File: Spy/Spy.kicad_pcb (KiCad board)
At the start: 2 copper layers, 8 parts, among them J1 Screw_Terminal_01x02, J2 Screw_Terminal_01x02, U1 ESP32-DevKitC, U2 GP2Y0A21YK0F, U3 GP2Y0A21YK0F, U4 SEN-12787, U5 L298N, U6 QTR-8A

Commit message: pcb edited
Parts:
- moved U5 48.9 mm to (94.2, 100.8), turned to 90 degrees
- moved J1 46.2 mm to (109.8, 86.0), turned to 180 degrees
- moved U1 39.6 mm to (130.1, 80.6)
- moved U2 39.1 mm to (107.7, 125.8)
- moved J2 31.8 mm to (85.0, 95.8), turned to -90 degrees
- moved U4 25.3 mm to (80.8, 116.5), turned to 90 degrees
- moved U3 24.3 mm to (97.7, 125.8)
- moved U6 15.0 mm to (135.0, 136.8)
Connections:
- J1 pad 1: unconnected-(J1-Pin_1-Pad1) -> Net-(J1-Pin_1)
- J1 pad 2: unconnected-(J1-Pin_2-Pad2) -> Net-(J1-Pin_2)
- J2 pad 1: unconnected-(J2-Pin_1-Pad1) -> Net-(J2-Pin_1)
- J2 pad 2: unconnected-(J2-Pin_2-Pad2) -> Net-(J2-Pin_2)
- U1 pad 1: unconnected-(U1-3V3-Pad1) -> Net-(U1-3V3)
- U1 pad 10: unconnected-(U1-DAC_2/ADC2_CH9/GPIO26-Pad10) -> Net-(U1-DAC_2/ADC2_CH9/GPIO26)
- U1 pad 12: unconnected-(U1-MTMS/GPIO14/ADC2_CH6-Pad12) -> Net-(U1-MTMS/GPIO14/ADC2_CH6)
- U1 pad 13: unconnected-(U1-MTDI/GPIO12/ADC2_CH5-Pad13) -> Net-(U1-MTDI/GPIO12/ADC2_CH5)
- U1 pad 14: Net-(U1-GND-Pad14) -> GND
- U1 pad 15: unconnected-(U1-MTCK/GPIO13/ADC2_CH4-Pad15) -> Net-(U1-MTCK/GPIO13/ADC2_CH4)
- U1 pad 19: unconnected-(U1-5V-Pad19) -> Net-(U1-5V)
- U1 pad 20: unconnected-(U1-SD_CLK/GPIO6-Pad20) -> Net-(U1-SD_CLK/GPIO6)
- U1 pad 21: unconnected-(U1-SD_DATA0/GPIO7-Pad21) -> Net-(U1-SD_DATA0/GPIO7)
- U1 pad 27: unconnected-(U1-GPIO16-Pad27) -> Net-(U1-GPIO16)
- U1 pad 28: unconnected-(U1-GPIO17-Pad28) -> Net-(U1-GPIO17)
- U1 pad 3: unconnected-(U1-SENSOR_VP/GPIO36/ADC1_CH0-Pad3) -> Net-(U1-SENSOR_VP/GPIO36/ADC1_CH0)
- U1 pad 30: unconnected-(U1-GPIO18-Pad30) -> Net-(U1-GPIO18)
- U1 pad 31: unconnected-(U1-GPIO19-Pad31) -> Net-(U1-GPIO19)
- U1 pad 32: Net-(U1-GND-Pad14) -> GND
- U1 pad 33: unconnected-(U1-GPIO21-Pad33) -> Net-(U1-GPIO21)
- U1 pad 36: unconnected-(U1-GPIO22-Pad36) -> Net-(U1-GPIO22)
- U1 pad 38: Net-(U1-GND-Pad14) -> GND
- U1 pad 5: unconnected-(U1-VDET_1/GPIO34/ADC1_CH6-Pad5) -> Net-(U1-VDET_1/GPIO34/ADC1_CH6)
- U1 pad 6: unconnected-(U1-VDET_2/GPIO35/ADC1_CH7-Pad6) -> Net-(U1-VDET_2/GPIO35/ADC1_CH7)
- U1 pad 7: unconnected-(U1-32K_XP/GPIO32/ADC1_CH4-Pad7) -> Net-(U1-32K_XP/GPIO32/ADC1_CH4)
- U1 pad 8: unconnected-(U1-32K_XN/GPIO33/ADC1_CH5-Pad8) -> Net-(U1-32K_XN/GPIO33/ADC1_CH5)
- U1 pad 9: unconnected-(U1-DAC_1/ADC2_CH8/GPIO25-Pad9) -> Net-(U1-DAC_1/ADC2_CH8/GPIO25)
- U2 pad 1: unconnected-(U2-GND-Pad1) -> GND
- U2 pad 2: unconnected-(U2-VCC-Pad2) -> Net-(U1-3V3)
- U2 pad 3: unconnected-(U2-VOUT-Pad3) -> Net-(U1-DAC_1/ADC2_CH8/GPIO25)
- U3 pad 1: unconnected-(U3-GND-Pad1) -> GND
- U3 pad 2: unconnected-(U3-VCC-Pad2) -> Net-(U1-3V3)
- U3 pad 3: unconnected-(U3-VOUT-Pad3) -> Net-(U1-DAC_2/ADC2_CH9/GPIO26)
- U4 pad 2: unconnected-(U4-GND-Pad2) -> GND
- U4 pad 3: unconnected-(U4-VCC-Pad3) -> Net-(U1-3V3)
- U4 pad 4: unconnected-(U4-SDA-Pad4) -> Net-(U1-SD_DATA0/GPIO7)
- U4 pad 5: unconnected-(U4-SCL-Pad5) -> Net-(U1-SD_CLK/GPIO6)
- U5 pad 10: unconnected-(U5-IN3-Pad10) -> Net-(U1-GPIO18)
- U5 pad 11: unconnected-(U5-ENB-Pad11) -> Net-(U1-GPIO22)
- U5 pad 12: unconnected-(U5-IN4-Pad12) -> Net-(U1-GPIO19)
- U5 pad 13: unconnected-(U5-OUT3-Pad13) -> Net-(J1-Pin_1)
- U5 pad 14: unconnected-(U5-OUT4-Pad14) -> Net-(J1-Pin_2)
- U5 pad 2: unconnected-(U5-OUT1-Pad2) -> Net-(J2-Pin_1)
- U5 pad 3: unconnected-(U5-OUT2-Pad3) -> Net-(J2-Pin_2)
- U5 pad 4: unconnected-(U5-VS-Pad4) -> Net-(U1-5V)
- U5 pad 5: unconnected-(U5-IN1-Pad5) -> Net-(U1-GPIO16)
- U5 pad 6: unconnected-(U5-ENA-Pad6) -> Net-(U1-GPIO21)
- U5 pad 7: unconnected-(U5-IN2-Pad7) -> Net-(U1-GPIO17)
- U5 pad 8: unconnected-(U5-GND-Pad8) -> GND
- U5 pad 9: unconnected-(U5-VSS-Pad9) -> +12V
- U6 pad 3V3: unconnected-(U6-Pad3V3) -> Net-(U1-3V3)
- U6 pad GND: unconnected-(U6-PadGND) -> GND
- U6 pad LED1: unconnected-(U6-PadLED1) -> Net-(U1-SENSOR_VP/GPIO36/ADC1_CH0)
- U6 pad LED2: unconnected-(U6-PadLED2) -> Net-(U1-VDET_2/GPIO35/ADC1_CH7)
- U6 pad LED3: unconnected-(U6-PadLED3) -> Net-(U1-VDET_1/GPIO34/ADC1_CH6)
- U6 pad LED4: unconnected-(U6-PadLED4) -> Net-(U1-MTMS/GPIO14/ADC2_CH6)
- U6 pad LED5: unconnected-(U6-PadLED5) -> Net-(U1-MTCK/GPIO13/ADC2_CH4)
- U6 pad LED6: unconnected-(U6-PadLED6) -> Net-(U1-MTDI/GPIO12/ADC2_CH5)
- U6 pad LED7: unconnected-(U6-PadLED7) -> Net-(U1-32K_XN/GPIO33/ADC1_CH5)
- U6 pad LED8: unconnected-(U6-PadLED8) -> Net-(U1-32K_XP/GPIO32/ADC1_CH4)
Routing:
- net GND: track 0.00 -> 197.8 mm
- net Net-(U1-5V): track 0.00 -> 107.5 mm
- net Net-(U1-SD_CLK/GPIO6): track 0.00 -> 100.1 mm
- net Net-(U1-3V3): track 0.00 -> 99.0 mm
- net Net-(U1-GPIO18): track 0.00 -> 97.8 mm, vias 0 -> 1
- net Net-(U1-SD_DATA0/GPIO7): track 0.00 -> 96.3 mm
- net Net-(U1-GPIO16): track 0.00 -> 75.3 mm, vias 0 -> 1
- net Net-(U1-GPIO21): track 0.00 -> 74.7 mm
- net Net-(U1-GPIO17): track 0.00 -> 70.3 mm, vias 0 -> 1
- net Net-(U1-VDET_1/GPIO34/ADC1_CH6): track 0.00 -> 70.3 mm
- net Net-(U1-GPIO19): track 0.00 -> 64.3 mm, vias 0 -> 1
- net Net-(U1-SENSOR_VP/GPIO36/ADC1_CH0): track 0.00 -> 61.3 mm
- net Net-(U1-GPIO22): track 0.00 -> 60.0 mm, vias 0 -> 1
- net Net-(U1-VDET_2/GPIO35/ADC1_CH7): track 0.00 -> 58.5 mm
- net Net-(U1-DAC_2/ADC2_CH9/GPIO26): track 0.00 -> 48.3 mm
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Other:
- board outline added: 96.8 x 80 mm

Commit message: new pcb
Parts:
- moved U4 96.0 mm to (174.8, 97.0), turned to -90 degrees
- moved J2 91.7 mm to (175.5, 80.8), turned to 180 degrees
- moved U6 75.8 mm to (63.0, 113.0), turned to -90 degrees
- moved J1 67.2 mm to (171.2, 113.2), turned to 0 degrees
- moved U2 66.4 mm to (73.2, 69.0)
- moved U1 63.7 mm to (73.1, 109.2), turned to 90 degrees
- moved U3 58.3 mm to (108.5, 68.5)
- moved U5 42.4 mm to (134.5, 87.8), turned to 0 degrees
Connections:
- net Net-(U1-32K_XN/GPIO33/ADC1_CH5) renamed GPIO33
- net Net-(U1-32K_XP/GPIO32/ADC1_CH4) renamed GPIO32
- net Net-(U1-3V3) renamed 3V3
- net Net-(U1-DAC_1/ADC2_CH8/GPIO25) renamed GPIO25
- net Net-(U1-DAC_2/ADC2_CH9/GPIO26) renamed GPIO26
- net Net-(U1-GPIO16) renamed GPIO16
- net Net-(U1-GPIO17) renamed GPIO17
- net Net-(U1-GPIO18) renamed GPIO18
- net Net-(U1-GPIO19) renamed GPIO19
- net Net-(U1-GPIO21) renamed GPIO21
- net Net-(U1-GPIO22) renamed GPIO22
- net Net-(U1-MTCK/GPIO13/ADC2_CH4) renamed GPIO13
- net Net-(U1-MTDI/GPIO12/ADC2_CH5) renamed GPIO12
- net Net-(U1-MTMS/GPIO14/ADC2_CH6) renamed GPIO14
- net Net-(U1-SD_CLK/GPIO6) renamed GPIO6
- net Net-(U1-SD_DATA0/GPIO7) renamed GPIO7
- net Net-(U1-SENSOR_VP/GPIO36/ADC1_CH0) renamed GPIO36
- net Net-(U1-VDET_1/GPIO34/ADC1_CH6) renamed GPIO34
- net Net-(U1-VDET_2/GPIO35/ADC1_CH7) renamed GPIO35
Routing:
- net 3V3: track 99.0 -> 216.1 mm
- net GND: track 197.8 -> 273.7 mm
- net Net-(U1-5V): track 107.5 -> 36.1 mm
- net GPIO18: track 97.8 -> 52.6 mm, vias 1 -> 0
- net GPIO16: track 75.3 -> 37.2 mm, vias 1 -> 0
- net Net-(J1-Pin_1): track 17.0 -> 47.5 mm
- net GPIO17: track 70.3 -> 40.8 mm, vias 1 -> 0
- net Net-(J2-Pin_1): track 10.4 -> 39.3 mm
- net Net-(J1-Pin_2): track 12.2 -> 40.5 mm
- net Net-(J2-Pin_2): track 13.9 -> 41.7 mm
- net GPIO13: track 26.1 -> 53.8 mm
- net GPIO26: track 48.3 -> 74.4 mm, vias 0 -> 1
- net GPIO34: track 70.3 -> 50.7 mm
- net GPIO12: track 32.0 -> 49.3 mm
- net GPIO32: track 47.4 -> 30.3 mm
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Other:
- board size 96.8 x 80 mm -> 134.2 x 76 mm

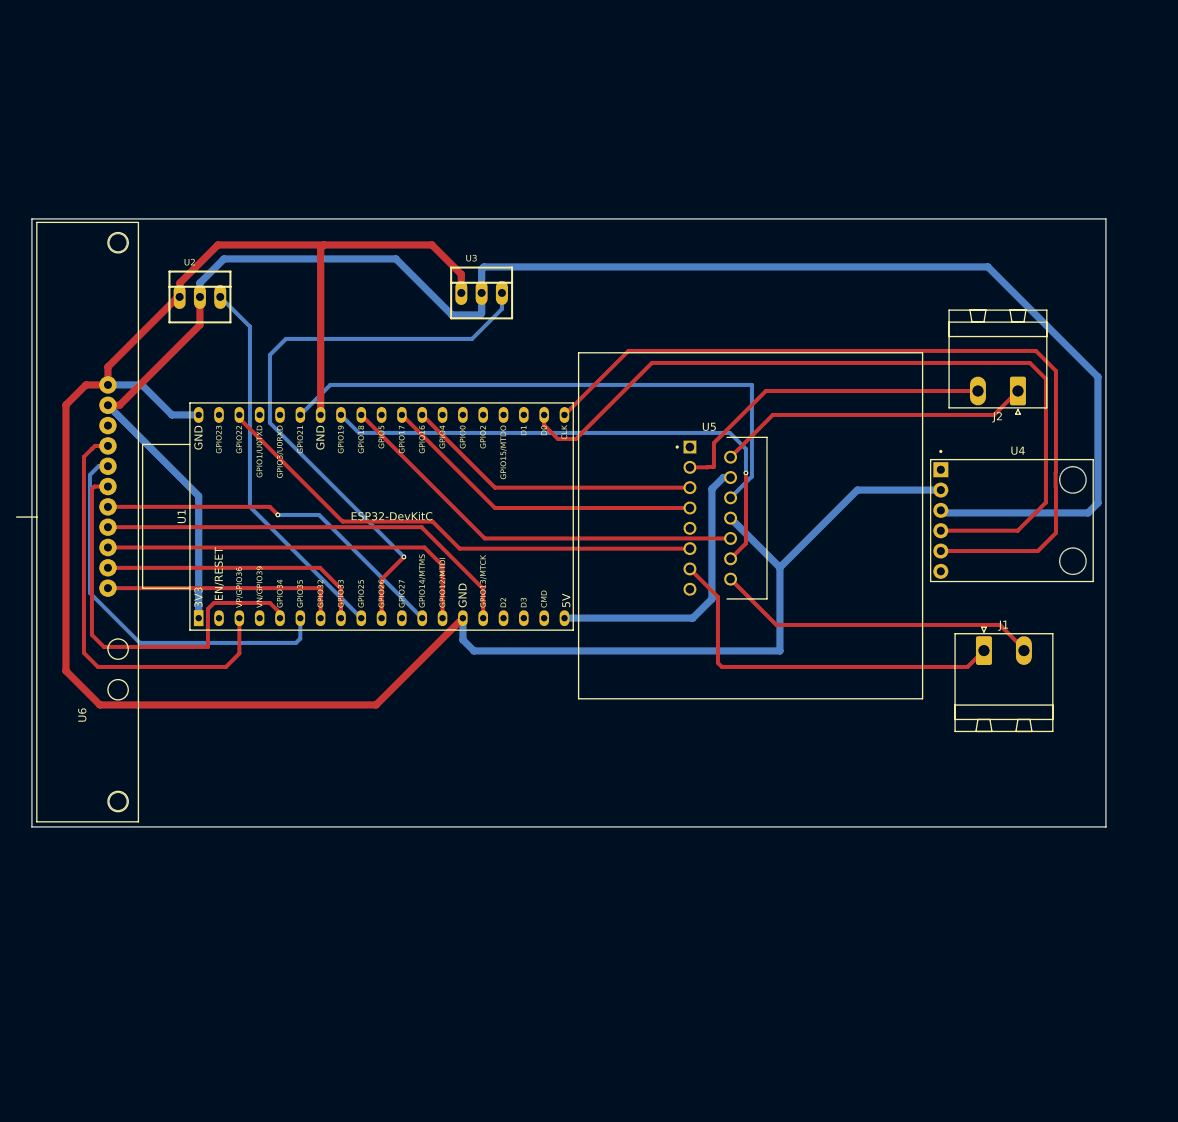
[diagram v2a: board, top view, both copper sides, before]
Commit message: DRV8871 driver and pin rewiring
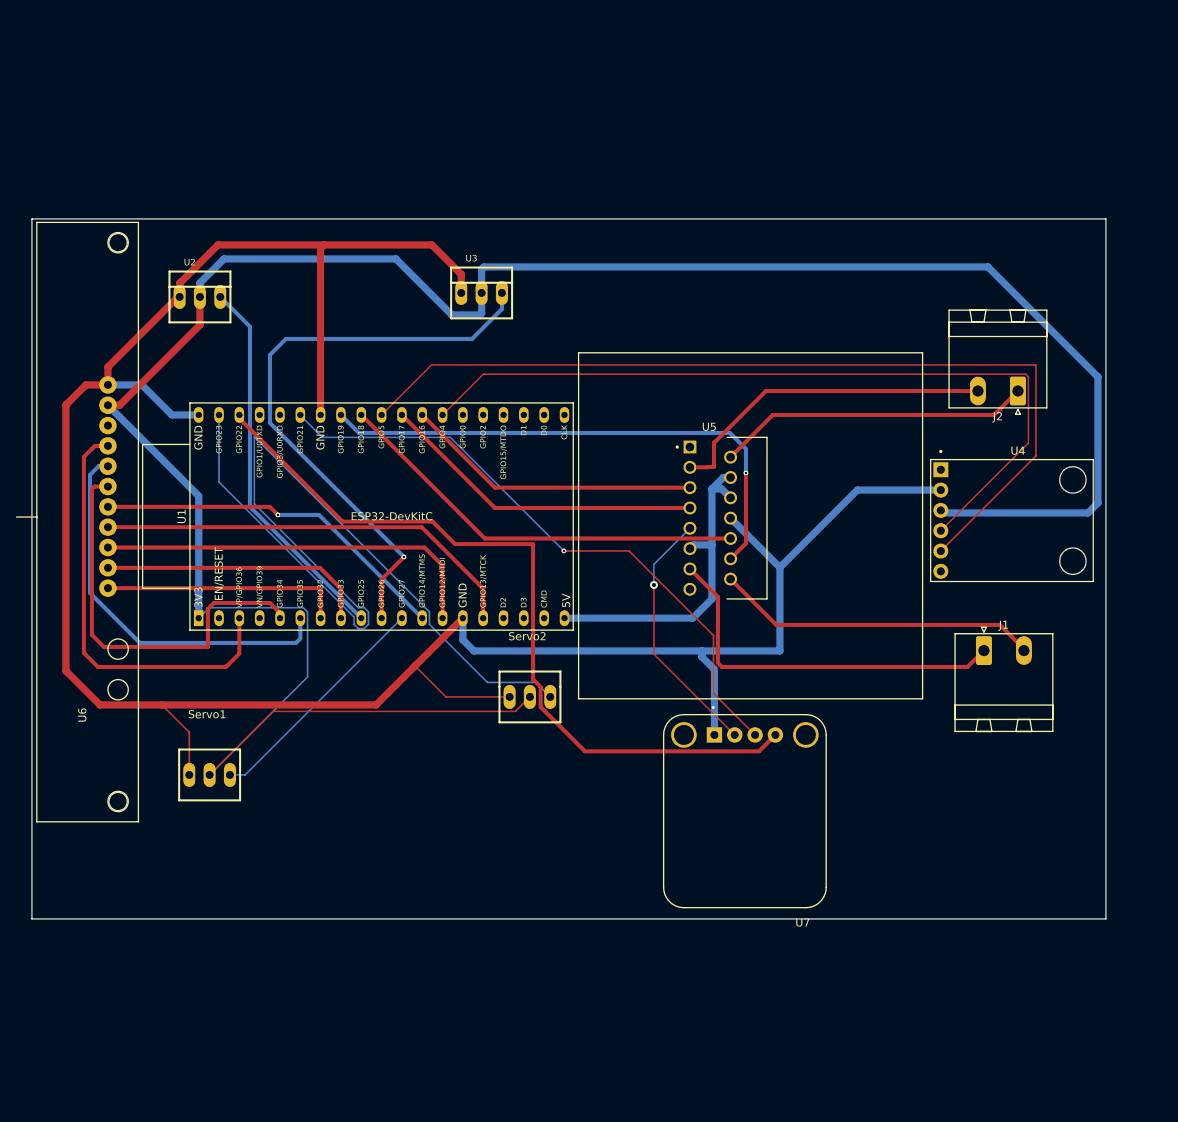
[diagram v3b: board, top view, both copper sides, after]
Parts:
- added Servo1: ~, FS5103B:FS5103B, F.Cu at (74.2, 121.7)
- added Servo2: ~, FS5103B:FS5103B, F.Cu at (114.2, 112.0)
- added U7: 3190, 3190:MODULE_3190, F.Cu at (141.4, 133.3)
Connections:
- U1 pad 11: unconnected-(U1-ADC2_CH7/GPIO27-Pad11) -> GPIO27
- U1 pad 20: GPIO6 -> unconnected-(U1-SD_CLK/GPIO6-Pad20)
- U1 pad 21: GPIO7 -> unconnected-(U1-SD_DATA0/GPIO7-Pad21)
- U1 pad 26: unconnected-(U1-ADC2_CH0/GPIO4-Pad26) -> GPIO4
- U1 pad 29: unconnected-(U1-GPIO5-Pad29) -> GPIO5
- U1 pad 37: unconnected-(U1-GPIO23-Pad37) -> GPIO23
- U4 pad 4: GPIO7 -> GPIO4
- U4 pad 5: GPIO6 -> GPIO5
- U5 pad 11: GPIO22 -> Net-(U1-5V)
- U5 pad 6: GPIO21 -> Net-(U1-5V)
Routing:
- net GPIO23: track 0.00 -> 117.1 mm
- net GPIO5: track 0.00 -> 112.6 mm
- net GPIO6: track 101.4 -> 0.00 mm
- net GPIO7: track 99.5 -> 0.00 mm
- net GPIO4: track 0.00 -> 99.2 mm
- net 3V3: track 216.1 -> 299.9 mm
- net GND: track 273.7 -> 308.5 mm
- net GPIO22: track 63.5 -> 96.9 mm
- net +12V: track 0.00 -> 31.9 mm, vias 0 -> 1
- net GPIO27: track 0.00 -> 29.6 mm
- net Net-(U1-5V): track 36.1 -> 42.0 mm
- net GPIO21: track 73.4 -> 77.7 mm, vias 0 -> 1
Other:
- board size 134.2 x 76 mm -> 134.2 x 87.5 mm

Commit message: rewired some stuff
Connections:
- U4 pad 4: GPIO4 -> GPIO21
- U4 pad 5: GPIO5 -> GPIO22
- U7 pad 3: GPIO21 -> GPIO4
- U7 pad 4: GPIO22 -> GPIO5
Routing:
- net GPIO21: track 77.7 -> 89.9 mm
- net GPIO22: track 96.9 -> 103.4 mm
- net GPIO5: track 112.6 -> 118.5 mm
- net GPIO4: track 99.2 -> 101.7 mm

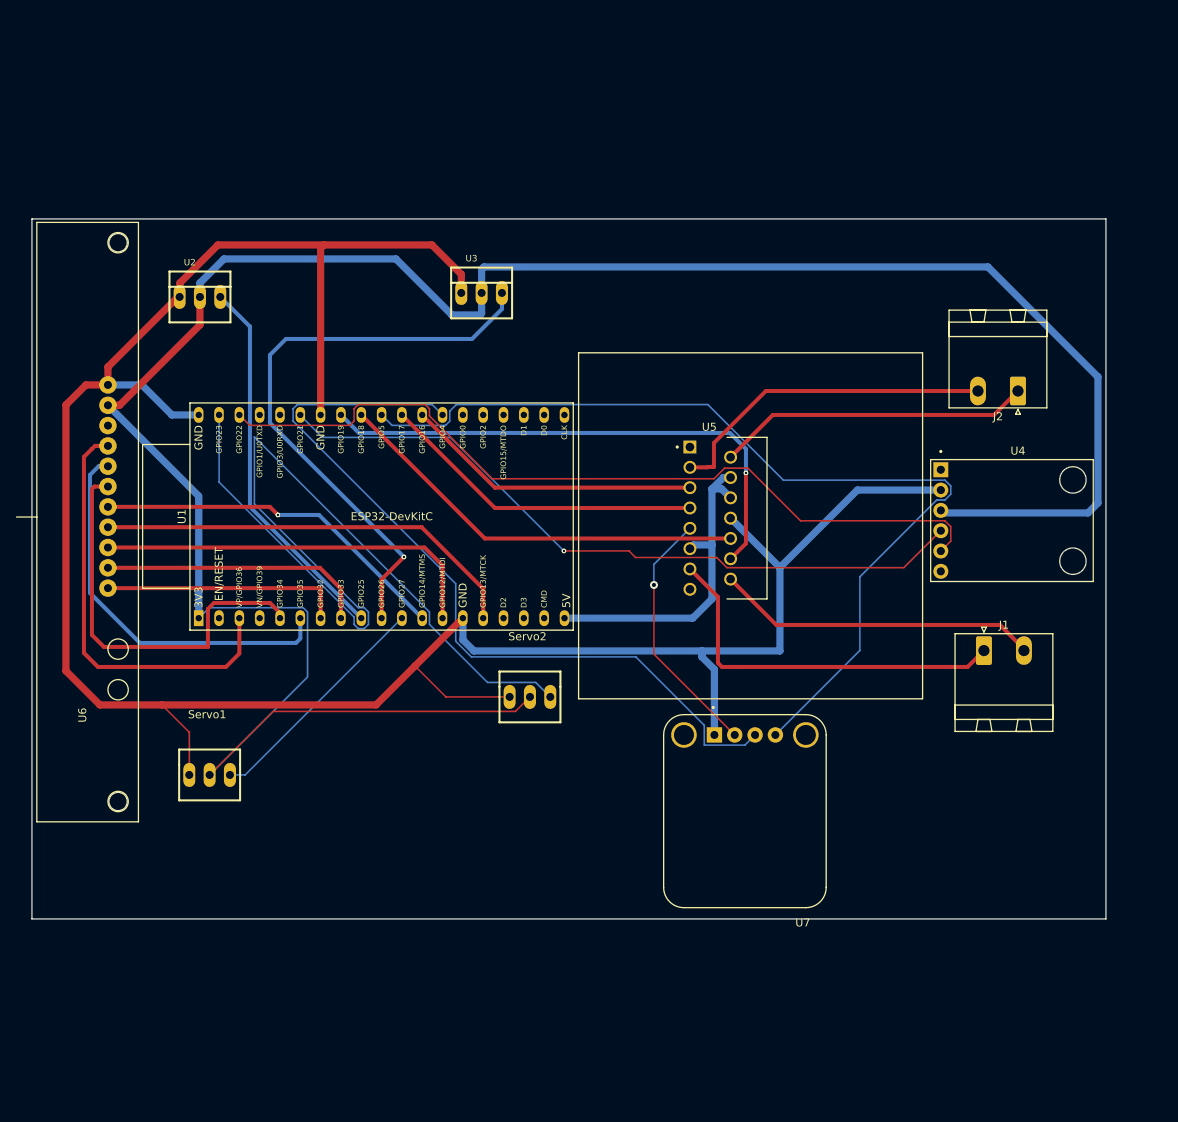
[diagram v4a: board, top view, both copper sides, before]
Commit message: Reverted and fixed version of code. Some minor PCB updates
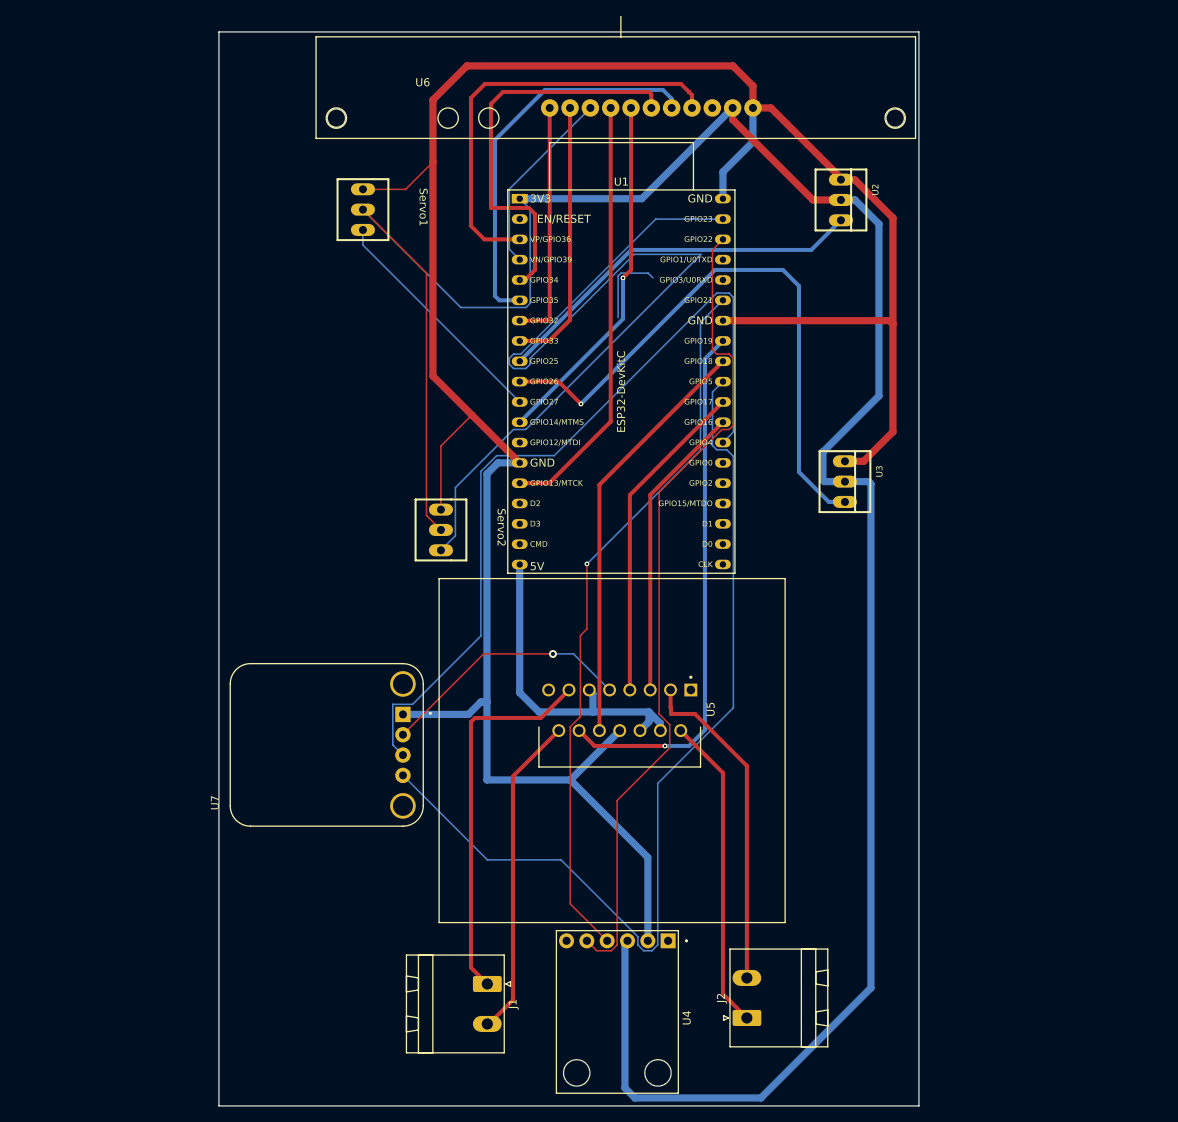
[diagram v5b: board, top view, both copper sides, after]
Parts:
- moved J2 85.4 mm to (141.6, 159.1), turned to 90 degrees
- moved U2 81.0 mm to (153.4, 56.9), turned to -90 degrees
- moved U6 80.9 mm to (109.4, 46.6), turned to 180 degrees
- moved U4 78.8 mm to (125.4, 158.4), turned to 180 degrees
- moved J1 74.8 mm to (109.2, 154.9), turned to -90 degrees
- moved Servo1 69.2 mm to (100.7, 57.8), turned to -90 degrees
- moved U1 66.0 mm to (113.2, 56.7), turned to 0 degrees
- moved U7 52.9 mm to (89.1, 125.0), turned to 90 degrees
- moved U3 51.2 mm to (153.9, 92.1), turned to -90 degrees
- moved U5 30.4 mm to (134.6, 118.1), turned to -90 degrees
- moved Servo2 14.6 mm to (110.4, 97.8), turned to -90 degrees
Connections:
- U1 pad 13: GPIO12 -> unconnected-(U1-MTDI/GPIO12/ADC2_CH5-Pad13)
- U1 pad 4: unconnected-(U1-SENSOR_VN/GPIO39/ADC1_CH3-Pad4) -> GPIO39
- U6 pad LED6: GPIO12 -> GPIO39
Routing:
- net GPIO12: track 49.3 -> 0.00 mm
- net GPIO39: track 0.00 -> 23.7 mm
- net (no net): track 0.00 -> 9.95 mm
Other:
- board size 134.2 x 87.5 mm -> 87.5 x 134.2 mm
- board text added: "GPIO12/MTDI"
